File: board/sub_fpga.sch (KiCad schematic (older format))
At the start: 11 parts, among them J1301 FPGA JTAG, Q1301 Q_NPN_BEC, U205 XC3S200-TQ144, X1301 SG7050CAN 25.0Mhz

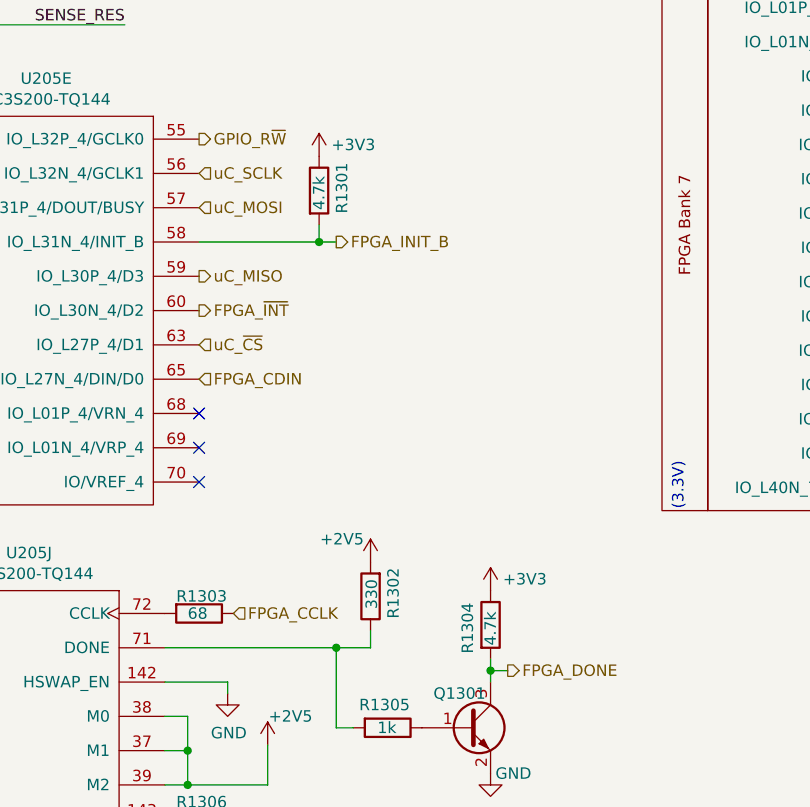
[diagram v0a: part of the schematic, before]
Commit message: Started picking footprints. Merged many components.
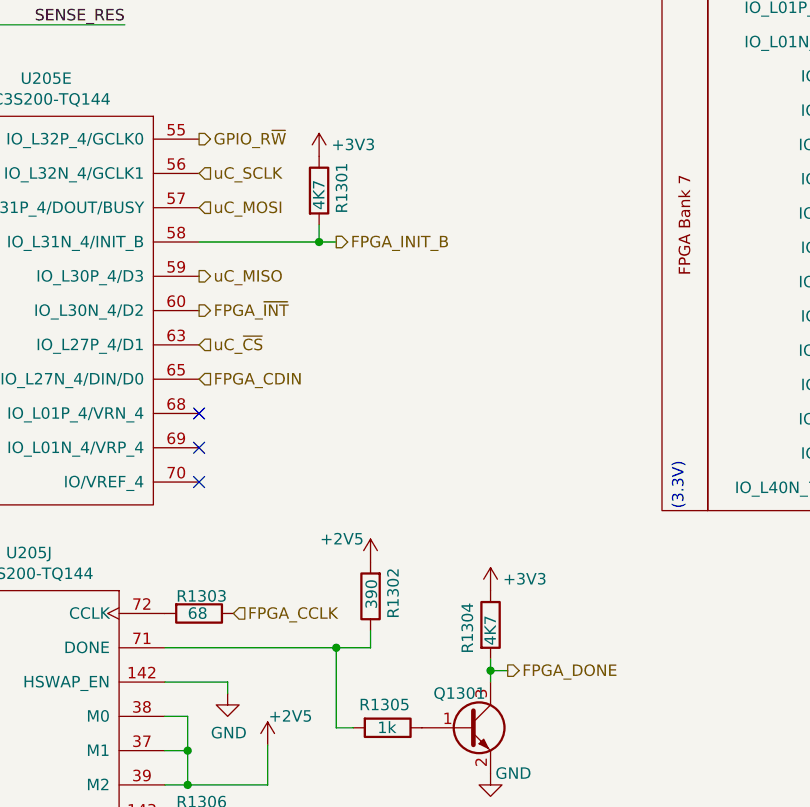
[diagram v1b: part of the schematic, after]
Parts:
- R1301, R1304: value 4.7k -> 4K7
- R1302: value 330 -> 390
- U205: footprint (none) -> Package_QFP:LQFP-144_20x20mm_P0.5mm
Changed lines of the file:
@@
 $Descr A4 11693 8268
 encoding utf-8
-Sheet 13 14
+Sheet 13 15
 Title ""
 Date ""
@@
 F 0 "U205" H 4656 5415 50  0000 C CNN
 F 1 "XC3S200-TQ144" H 4656 5324 50  0000 C CNN
-F 2 "" H 4425 4600 50  0001 C CNN
+F 2 "Package_QFP:LQFP-144_20x20mm_P0.5mm" H 4425 4600 50  0001 C CNN
 F 3 "" H 4425 4600 50  0001 C CNN
 	5    4875 4500
@@
 F 0 "U205" H 10306 2965 50  0000 C CNN
 F 1 "XC3S200-TQ144" H 10306 2874 50  0000 C CNN
-F 2 "" H 10000 2150 50  0001 C CNN
+F 2 "Package_QFP:LQFP-144_20x20mm_P0.5mm" H 10000 2150 50  0001 C CNN
 F 3 "" H 10000 2150 50  0001 C CNN
 	4    10450 2050
@@
 F 0 "U205" H 10306 5565 50  0000 C CNN
 F 1 "XC3S200-TQ144" H 10306 5474 50  0000 C CNN
-F 2 "" H 10000 4750 50  0001 C CNN
+F 2 "Package_QFP:LQFP-144_20x20mm_P0.5mm" H 10000 4750 50  0001 C CNN
 F 3 "" H 10000 4750 50  0001 C CNN
 	3    10450 4650
@@
 F 0 "U205" H 7956 2565 50  0000 C CNN
 F 1 "XC3S200-TQ144" H 7956 2474 50  0000 C CNN
-F 2 "" H 7650 1750 50  0001 C CNN
+F 2 "Package_QFP:LQFP-144_20x20mm_P0.5mm" H 7650 1750 50  0001 C CNN
 F 3 "" H 7650 1750 50  0001 C CNN
 	2    8100 1650
@@
 F 0 "U205" H 5856 2565 50  0000 C CNN
 F 1 "XC3S200-TQ144" H 5856 2474 50  0000 C CNN
-F 2 "" H 5550 1750 50  0001 C CNN
+F 2 "Package_QFP:LQFP-144_20x20mm_P0.5mm" H 5550 1750 50  0001 C CNN
 F 3 "" H 5550 1750 50  0001 C CNN
 	1    6000 1650
@@
 F 0 "U205" H 7956 4840 50  0000 C CNN
 F 1 "XC3S200-TQ144" H 7956 4749 50  0000 C CNN
-F 2 "" H 7650 4025 50  0001 C CNN
+F 2 "Package_QFP:LQFP-144_20x20mm_P0.5mm" H 7650 4025 50  0001 C CNN
 F 3 "" H 7650 4025 50  0001 C CNN
 	8    8100 3925
@@
 F 0 "U205" H 4581 7490 50  0000 C CNN
 F 1 "XC3S200-TQ144" H 4581 7399 50  0000 C CNN
-F 2 "" H 4275 6675 50  0001 C CNN
+F 2 "Package_QFP:LQFP-144_20x20mm_P0.5mm" H 4275 6675 50  0001 C CNN
 F 3 "" H 4275 6675 50  0001 C CNN
 	10   4725 6575
@@
 F 0 "U205" H 1256 5415 50  0000 C CNN
 F 1 "XC3S200-TQ144" H 1256 5324 50  0000 C CNN
-F 2 "" H 950 4600 50  0001 C CNN
+F 2 "Package_QFP:LQFP-144_20x20mm_P0.5mm" H 950 4600 50  0001 C CNN
 F 3 "" H 950 4600 50  0001 C CNN
 	7    1400 4500
@@
 F 0 "U205" H 1331 7915 50  0000 C CNN
 F 1 "XC3S200-TQ144" H 1331 7824 50  0000 C CNN
-F 2 "" H 950 7100 50  0001 C CNN
+F 2 "Package_QFP:LQFP-144_20x20mm_P0.5mm" H 950 7100 50  0001 C CNN
 F 3 "" H 950 7100 50  0001 C CNN
 	6    1400 7000
@@
 P 6075 5850
 F 0 "R1302" V 5975 5725 50  0000 L CNN
-F 1 "330" V 6070 5775 50  0000 L CNN
+F 1 "390" V 6070 5775 50  0000 L CNN
 F 2 "" V 6005 5850 50  0001 C CNN
 F 3 "~" H 6075 5850 50  0001 C CNN
@@
 P 6600 5975
 F 0 "R1304" V 6500 5850 50  0000 L CNN
-F 1 "4.7k" V 6600 5885 50  0000 L CNN
+F 1 "4K7" V 6600 5885 50  0000 L CNN
 F 2 "" V 6530 5975 50  0001 C CNN
 F 3 "~" H 6600 5975 50  0001 C CNN
@@
 P 5850 4075
 F 0 "R1301" V 5950 3975 50  0000 L CNN
-F 1 "4.7k" V 5850 3990 50  0000 L CNN
+F 1 "4K7" V 5850 3990 50  0000 L CNN
 F 2 "" V 5780 4075 50  0001 C CNN
 F 3 "~" H 5850 4075 50  0001 C CNN

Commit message: More footprints done. Went with simpler test-pads.
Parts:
- J1301: footprint (none) -> Connector_PinHeader_2.54mm:PinHeader_1x06_P2.54mm_Vertical
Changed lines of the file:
@@
 $Descr A4 11693 8268
 encoding utf-8
-Sheet 13 15
+Sheet 13 14
 Title ""
 Date ""
@@
 F 0 "J1301" V 6750 6775 50  0000 L CNN
 F 1 "FPGA JTAG" H 6300 6725 50  0000 L CNN
-F 2 "" H 6650 7150 50  0001 C CNN
+F 2 "Connector_PinHeader_2.54mm:PinHeader_1x06_P2.54mm_Vertical" H 6650 7150 50  0001 C CNN
 F 3 "~" H 6650 7150 50  0001 C CNN
 	1    6650 7150

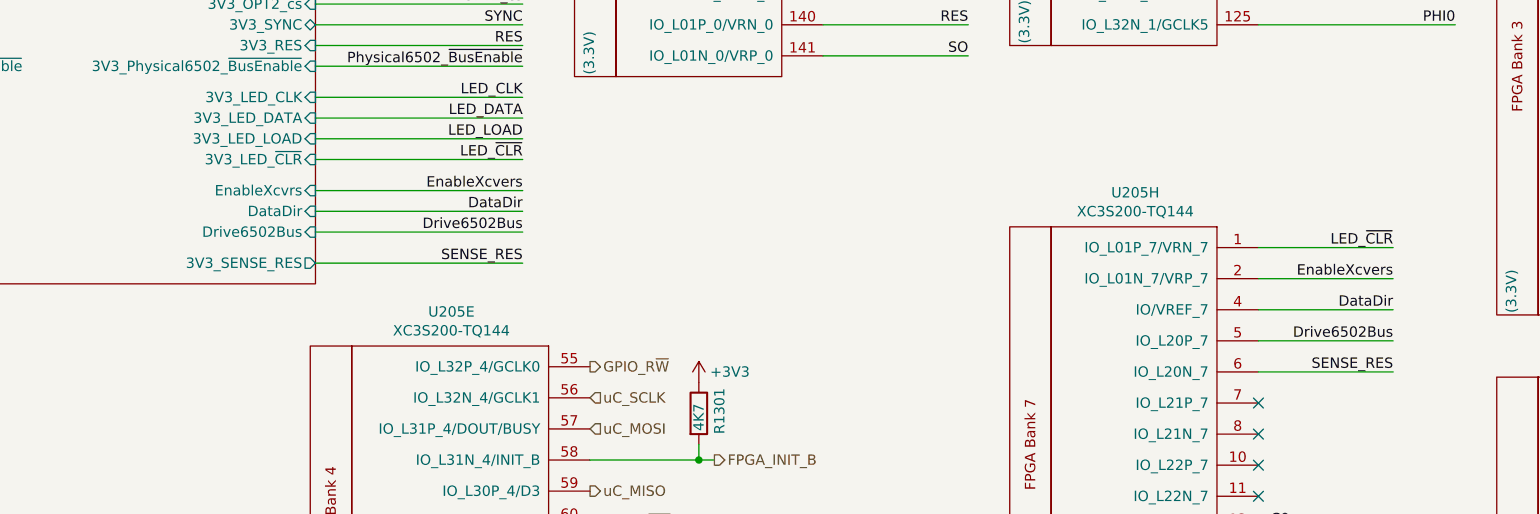
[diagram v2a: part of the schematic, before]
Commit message: Fixed swapped pin and some labels
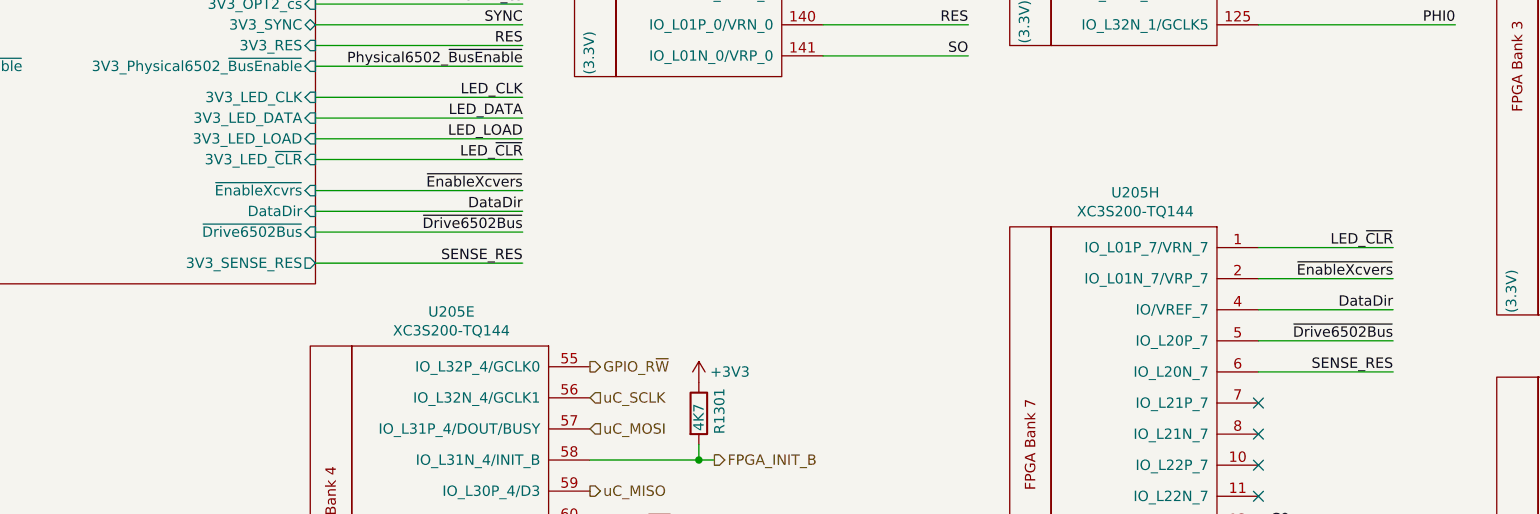
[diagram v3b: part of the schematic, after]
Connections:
- net Drive6502Bus renamed ~Drive6502Bus
- net EnableXcvers renamed ~EnableXcvers
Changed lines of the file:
@@
 F34 "5V_LED_DATA" O L 1550 2650 50
 F35 "5V_LED_LOAD" O L 1550 2750 50
-F36 "EnableXcvrs" I R 4000 3000 50
-F37 "Drive6502Bus" I R 4000 3200 50
-F38 "DataDir" I R 4000 3100 50
-F39 "3V3_LED_CLK" I R 4000 2550 50
-F40 "3V3_LED_DATA" I R 4000 2650 50
-F41 "3V3_LED_LOAD" I R 4000 2750 50
-F42 "3V3_LED_~CLR" I R 4000 2850 50
-F43 "5V_LED_~CLR" O L 1550 2850 50
-F44 "3V3_IRQ" I R 4000 1500 50
-F45 "3V3_RES" I R 4000 2300 50
-F46 "3V3_SENSE_RES" O R 4000 3350 50
-F47 "3V3_DATA[7..0]" T R 4000 800 50
+F36 "DataDir" I R 4000 3100 50
+F37 "3V3_LED_CLK" I R 4000 2550 50
+F38 "3V3_LED_DATA" I R 4000 2650 50
+F39 "3V3_LED_LOAD" I R 4000 2750 50
+F40 "3V3_LED_~CLR" I R 4000 2850 50
+F41 "5V_LED_~CLR" O L 1550 2850 50
+F42 "3V3_IRQ" I R 4000 1500 50
+F43 "3V3_RES" I R 4000 2300 50
+F44 "3V3_SENSE_RES" O R 4000 3350 50
+F45 "3V3_DATA[7..0]" T R 4000 800 50
+F46 "~EnableXcvrs" I R 4000 3000 50
+F47 "~Drive6502Bus" I R 4000 3200 50
 $EndSheet
 Text HLabel 1500 2550 0    50   Output ~ 0
@@
 LED_~CLR
 Text Label 5000 3000 2    50   ~ 0
-EnableXcvers
+~EnableXcvers
 Text Label 5000 2650 2    50   ~ 0
 LED_DATA
@@
 Physical6502_~BusEnable
 Text Label 5000 3200 2    50   ~ 0
-Drive6502Bus
+~Drive6502Bus
 Text Label 5000 3350 2    50   ~ 0
 SENSE_RES
@@
 LED_~CLR
 Text Label 9200 3425 2    50   ~ 0
-EnableXcvers
+~EnableXcvers
 Text Label 9500 1900 2    50   ~ 0
 LED_DATA
@@
 Physical6502_~BusEnable
 Text Label 9200 3725 2    50   ~ 0
-Drive6502Bus
+~Drive6502Bus
 Text Label 9200 3875 2    50   ~ 0
 SENSE_RES

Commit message: Most footprints associated
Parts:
- C1301: footprint (none) -> Capacitor_SMD:C_0603_1608Metric
- Q1301: footprint (none) -> Package_TO_SOT_SMD:SOT-23
- R1301, R1302, R1303, R1304, R1305, R1306: footprint (none) -> Resistor_SMD:R_0603_1608Metric
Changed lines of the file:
@@
 F 0 "C1301" H 3365 7496 50  0000 L CNN
 F 1 "0.1u" H 3365 7405 50  0000 L CNN
-F 2 "" H 3288 7300 50  0001 C CNN
+F 2 "Capacitor_SMD:C_0603_1608Metric" H 3288 7300 50  0001 C CNN
 F 3 "~" H 3250 7450 50  0001 C CNN
 	1    3250 7450
@@
 F 0 "R1303" V 5250 5825 50  0000 L CNN
 F 1 "68" V 5325 5875 50  0000 L CNN
-F 2 "" V 5255 5925 50  0001 C CNN
+F 2 "Resistor_SMD:R_0603_1608Metric" V 5255 5925 50  0001 C CNN
 F 3 "~" H 5325 5925 50  0001 C CNN
 	1    5325 5925
@@
 F 0 "R1302" V 5975 5725 50  0000 L CNN
 F 1 "390" V 6070 5775 50  0000 L CNN
-F 2 "" V 6005 5850 50  0001 C CNN
+F 2 "Resistor_SMD:R_0603_1608Metric" V 6005 5850 50  0001 C CNN
 F 3 "~" H 6075 5850 50  0001 C CNN
 	1    6075 5850
@@
 F 0 "R1306" V 5250 6725 50  0000 L CNN
 F 1 "68" V 5325 6775 50  0000 L CNN
-F 2 "" V 5255 6825 50  0001 C CNN
+F 2 "Resistor_SMD:R_0603_1608Metric" V 5255 6825 50  0001 C CNN
 F 3 "~" H 5325 6825 50  0001 C CNN
 	1    5325 6825
@@
 F 0 "Q1301" H 6350 6575 50  0000 L CNN
 F 1 "Q_NPN_BEC" H 6691 6380 50  0001 L CNN
-F 2 "" H 6700 6525 50  0001 C CNN
+F 2 "Package_TO_SOT_SMD:SOT-23" H 6700 6525 50  0001 C CNN
 F 3 "~" H 6500 6425 50  0001 C CNN
 	1    6500 6425
@@
 F 0 "R1304" V 6500 5850 50  0000 L CNN
 F 1 "4K7" V 6600 5885 50  0000 L CNN
-F 2 "" V 6530 5975 50  0001 C CNN
+F 2 "Resistor_SMD:R_0603_1608Metric" V 6530 5975 50  0001 C CNN
 F 3 "~" H 6600 5975 50  0001 C CNN
 	1    6600 5975
@@
 F 0 "R1305" V 6050 6300 50  0000 L CNN
 F 1 "1k" V 6150 6380 50  0000 L CNN
-F 2 "" V 6080 6425 50  0001 C CNN
+F 2 "Resistor_SMD:R_0603_1608Metric" V 6080 6425 50  0001 C CNN
 F 3 "~" H 6150 6425 50  0001 C CNN
 	1    6150 6425
@@
 F 0 "R1301" V 5950 3975 50  0000 L CNN
 F 1 "4K7" V 5850 3990 50  0000 L CNN
-F 2 "" V 5780 4075 50  0001 C CNN
+F 2 "Resistor_SMD:R_0603_1608Metric" V 5780 4075 50  0001 C CNN
 F 3 "~" H 5850 4075 50  0001 C CNN
 	1    5850 4075

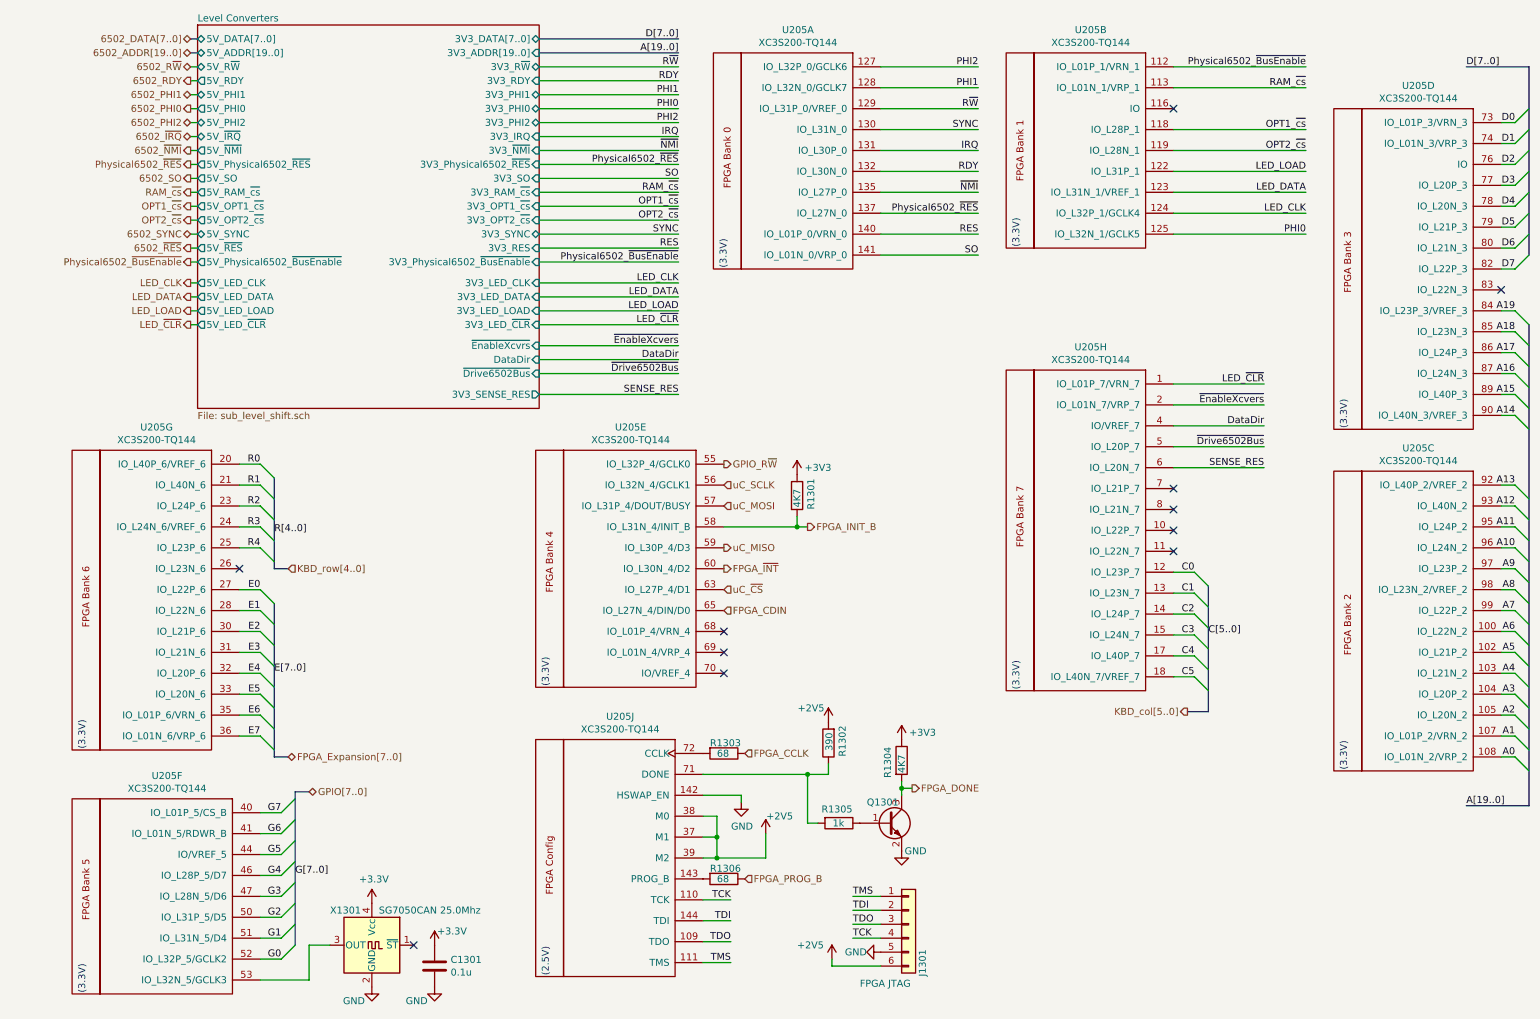
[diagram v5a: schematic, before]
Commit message: Power supply routed
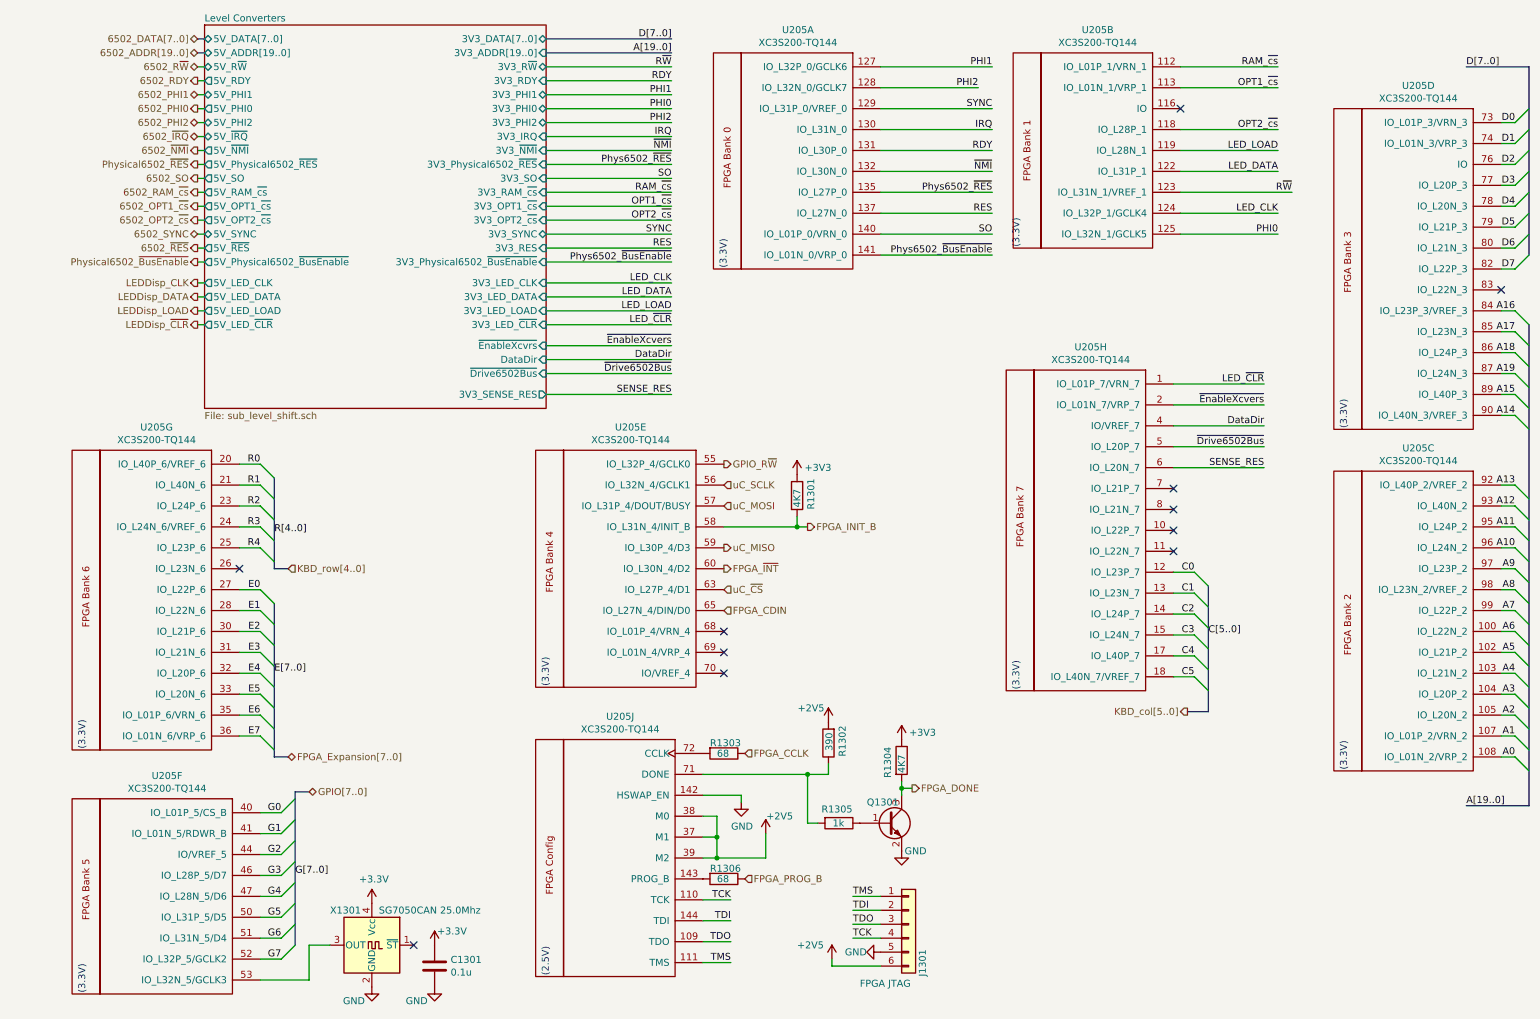
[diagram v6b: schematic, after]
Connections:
- net A16: now also U205.84 (IO_L23P_3/VREF_3); no longer U205.87 (IO_L24N_3)
- net A17: now also U205.85 (IO_L23N_3); no longer U205.86 (IO_L24P_3)
- net A18: now also U205.86 (IO_L24P_3); no longer U205.85 (IO_L23N_3)
- net A19: now also U205.87 (IO_L24N_3); no longer U205.84 (IO_L23P_3/VREF_3)
- net G0: now also U205.40 (IO_L01P_5/CS_B); no longer U205.52 (IO_L32P_5/GCLK2)
- net G1: now also U205.41 (IO_L01N_5/RDWR_B); no longer U205.51 (IO_L31N_5/D4)
- net G2: now also U205.44 (IO/VREF_5); no longer U205.50 (IO_L31P_5/D5)
- net G3: now also U205.46 (IO_L28P_5/D7); no longer U205.47 (IO_L28N_5/D6)
- net G4: now also U205.47 (IO_L28N_5/D6); no longer U205.46 (IO_L28P_5/D7)
- net G5: now also U205.50 (IO_L31P_5/D5); no longer U205.44 (IO/VREF_5)
- net G6: now also U205.51 (IO_L31N_5/D4); no longer U205.41 (IO_L01N_5/RDWR_B)
- net G7: now also U205.52 (IO_L32P_5/GCLK2); no longer U205.40 (IO_L01P_5/CS_B)
- net IRQ: now also U205.130 (IO_L31N_0); no longer U205.131 (IO_L30P_0)
- net LED_DATA: now also U205.122 (IO_L31P_1); no longer U205.123 (IO_L31N_1/VREF_1)
- net LED_LOAD: now also U205.119 (IO_L28N_1); no longer U205.122 (IO_L31P_1)
- net OPT1_~cs: now also U205.113 (IO_L01N_1/VRP_1); no longer U205.118 (IO_L28P_1)
- net OPT2_~cs: now also U205.118 (IO_L28P_1); no longer U205.119 (IO_L28N_1)
- net PHI1: now also U205.127 (IO_L32P_0/GCLK6); no longer U205.128 (IO_L32N_0/GCLK7)
- net PHI2: now also U205.128 (IO_L32N_0/GCLK7); no longer U205.127 (IO_L32P_0/GCLK6)
- net Physical6502_~BusEnable: no longer U205.112 (IO_L01P_1/VRN_1)
- net Physical6502_~RES: no longer U205.137 (IO_L27N_0)
- net RAM_~cs: now also U205.112 (IO_L01P_1/VRN_1); no longer U205.113 (IO_L01N_1/VRP_1)
- net RDY: now also U205.131 (IO_L30P_0); no longer U205.132 (IO_L30N_0)
- net RES: now also U205.137 (IO_L27N_0); no longer U205.140 (IO_L01P_0/VRN_0)
- net R~W: now also U205.123 (IO_L31N_1/VREF_1); no longer U205.129 (IO_L31P_0/VREF_0)
- net SO: now also U205.140 (IO_L01P_0/VRN_0); no longer U205.141 (IO_L01N_0/VRP_0)
- net SYNC: now also U205.129 (IO_L31P_0/VREF_0); no longer U205.130 (IO_L31N_0)
- net ~NMI: now also U205.132 (IO_L30N_0); no longer U205.135 (IO_L27P_0)
- new net Phys6502_~BusEnable: U205.141 (IO_L01N_0/VRP_0)
- new net Phys6502_~RES: U205.135 (IO_L27P_0)
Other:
- moved on the sheet: U205B
